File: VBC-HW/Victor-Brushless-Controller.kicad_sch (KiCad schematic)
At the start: 81 parts, among them J1 i2c QWIIC, P1 PVDD, P2 GND, Q1 TPH4R008NH, Q2 TPH4R008NH, Q3 TPH4R008NH, Q4 TPH4R008NH, Q5 TPH4R008NH, Q6 TPH4R008NH, SW1 SW_SPST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

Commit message: Preliminary component placing
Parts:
- PA1: value Phase -> A
- PB1: value Phase -> B
- PC1: value Phase -> C
- SW1: value SW_SPST -> BOOT
- SW2: value SW_SPST -> RESET

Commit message: Updated PCB and code
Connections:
- net IO15 is gone; now on net IO 15: U2.23 (IO15)

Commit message: Updates connections in board
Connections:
- net IO 15 renamed IO15

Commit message: Starting added traces to board
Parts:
- JP1: value SolderJumper -> 3V3
- P1: value PVDD -> V+
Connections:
- net BOOT IO0: now also H2.4 (Pin_4); no longer H2.1 (Pin_1)
- net GND: now also U2.39 (P_GND)
- net RESET EN: now also H2.3 (Pin_3); no longer H2.2 (Pin_2)
- net RX0: now also H2.2 (Pin_2); no longer H2.3 (Pin_3)
- net TX0: now also H2.1 (Pin_1); no longer H2.4 (Pin_4)
- no-connect marks 14 -> 13
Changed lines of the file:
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@@
 (kicad_sch
-	(version 20231120)
+	(version 20250114)
 	(generator "eeschema")
-	(generator_version "8.0")
+	(generator_version "9.0")
 	(paper "A4")
 	(title_block

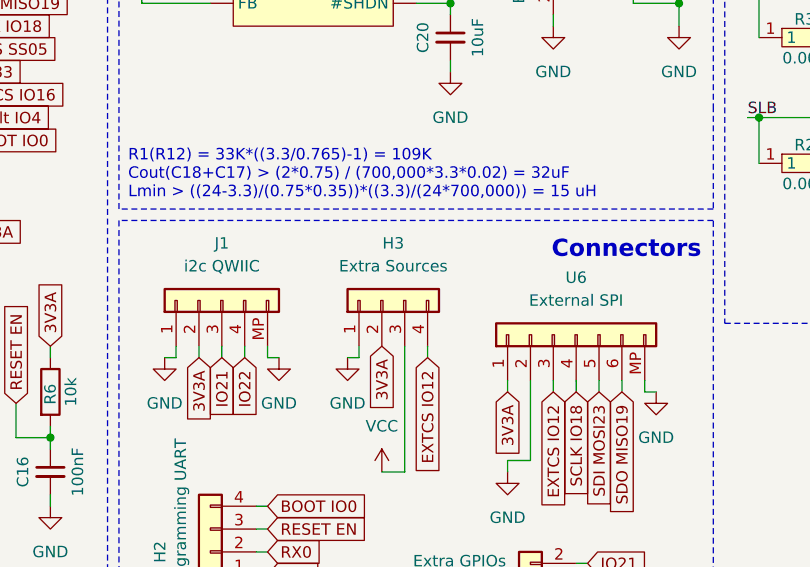
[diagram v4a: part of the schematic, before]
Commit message: Finished vias and Inner layer 1
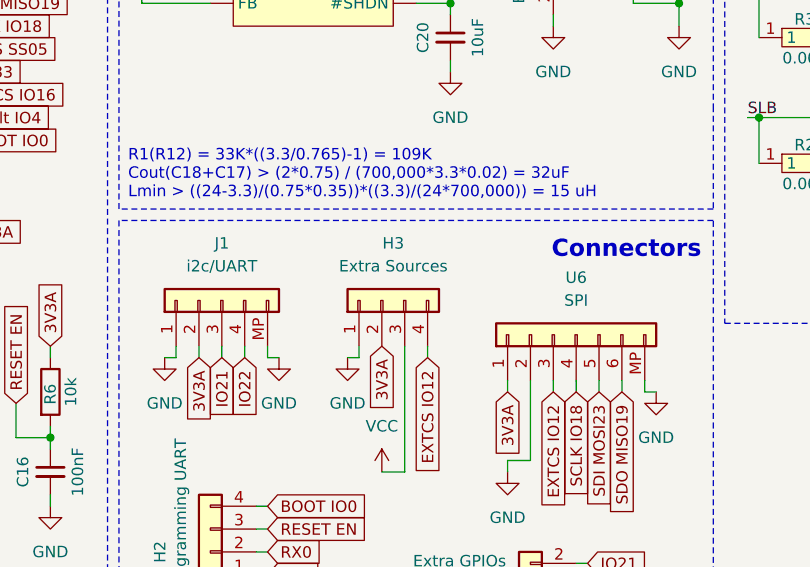
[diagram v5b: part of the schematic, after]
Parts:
- J1: value i2c QWIIC -> i2c/UART
- U6: value External SPI -> SPI

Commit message: Finished all connections
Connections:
- net EN I02 is gone; now on net EN IO2: U1.1 (EN_GATE)
- net 3V3A: now also J1.3 (Pin_3), U6.6 (Pin_6); no longer J1.2 (Pin_2), U6.1 (Pin_1)
- net EXTCS IO12: now also U6.4 (Pin_4); no longer U6.3 (Pin_3)
- net GND: now also J1.4 (Pin_4), U6.5 (Pin_5); no longer J1.1 (Pin_1), U6.2 (Pin_2)
- net IO21: now also J1.2 (Pin_2); no longer J1.3 (Pin_3)
- net IO22: now also J1.1 (Pin_1); no longer J1.4 (Pin_4)
- net SCLK IO18: now also U6.3 (Pin_3); no longer U6.4 (Pin_4)
- net SDI MOSI23: now also U6.2 (Pin_2); no longer U6.5 (Pin_5)
- net SDO MISO19: now also U6.1 (Pin_1); no longer U6.6 (Pin_6)
